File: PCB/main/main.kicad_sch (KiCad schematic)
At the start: 4 parts

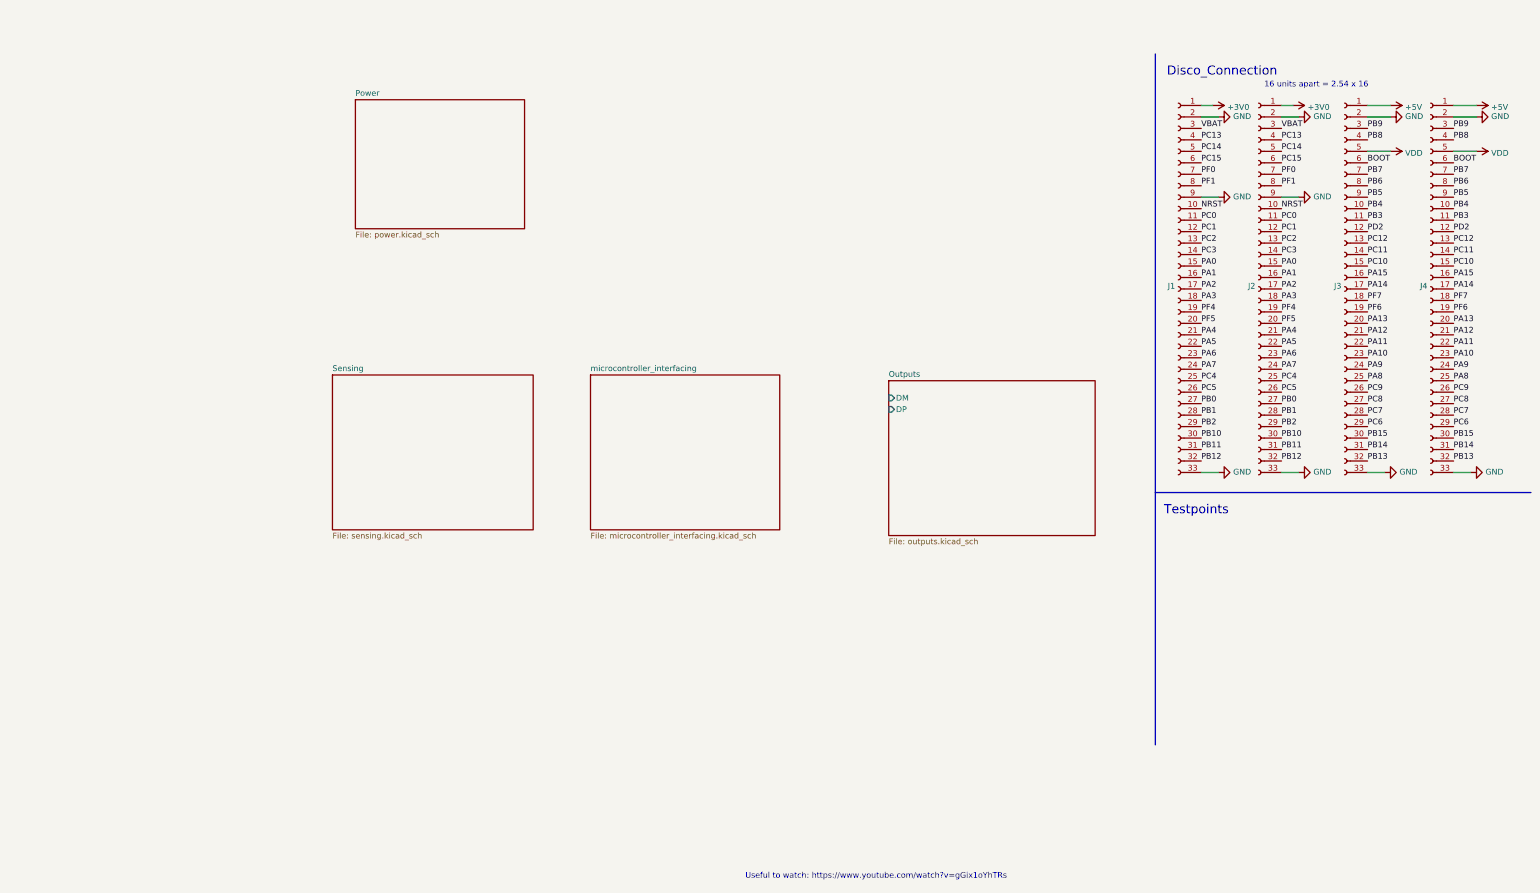
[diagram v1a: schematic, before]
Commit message: added digital sensors
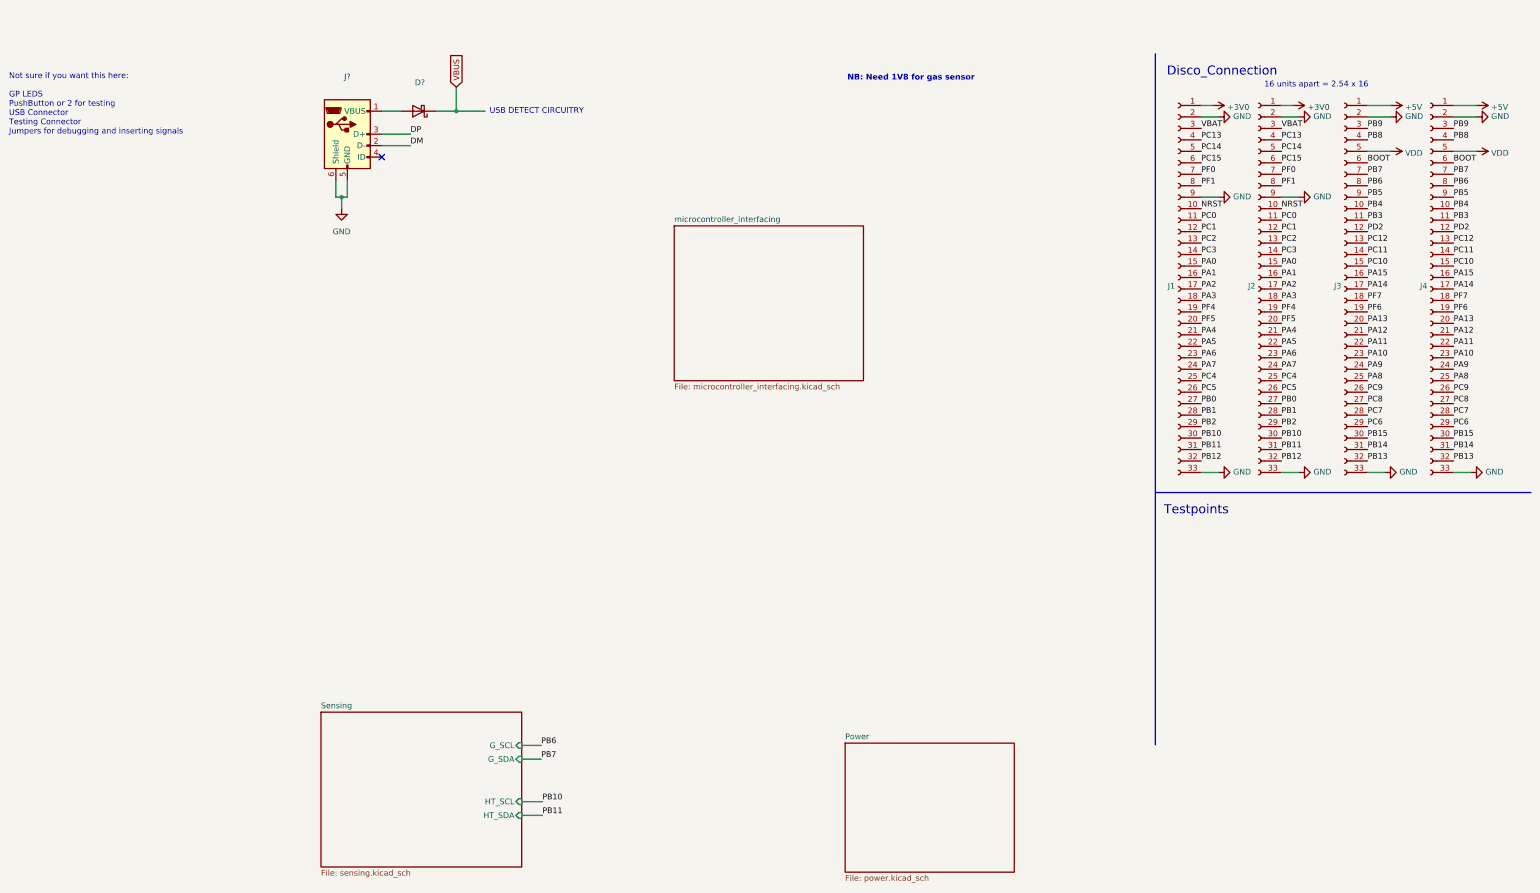
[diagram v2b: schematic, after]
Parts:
- added D?: (no value), symbol Device:D_Schottky
- added J?: (no value), symbol Connector:USB_B_Micro
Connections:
- net GND: now also J?.5 (GND), J?.6 (Shield)
- new net: D?.2 (A), J?.1 (VBUS)
- new net DM: J?.2 (D-)
- new net DP: J?.3 (D+)
- new net VBUS: D?.1 (K)
- no-connect marks 0 -> 1
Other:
- removed sheet Outputs
- sheet Sensing ports: added G_SCL, G_SDA, HT_SCL, HT_SDA; removed none
- note added: "NB: Need 1V8 for gas sensor"
- note added: "Not sure if you want this here: GP LEDS PushButton or 2 for testing USB Connector Testing Connector Jumpers for debugging and inserting signals"
- note added: "USB DETECT CIRCUITRY"
- note removed: "Useful to watch: https://www.youtube.com/watch?v=gGix1oYhTRs"
- title: EEE3088F Template -> DiscoverAir HAT

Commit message: added eeprom and some usb-uart connections
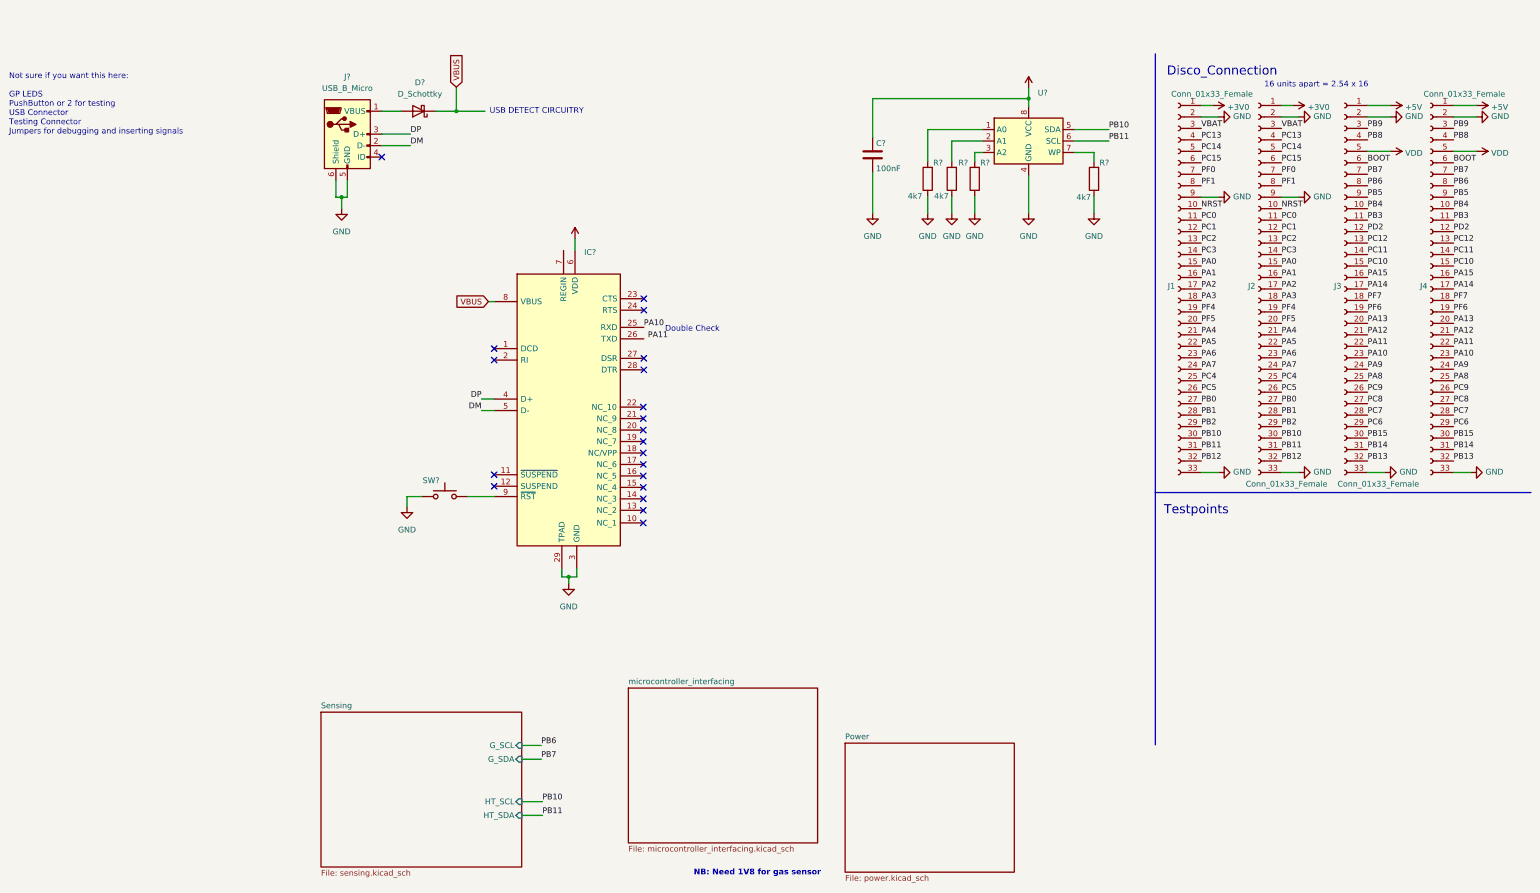
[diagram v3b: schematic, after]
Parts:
- added C?: 100nF, Capacitor_SMD:C_0603_1608Metric_Pad1.08x0.95mm_HandSolder, symbol Device:C
- added IC?: (no value), symbol CP2102-GMR:CP2102-GMR
- added R?: (no value), symbol Device:R
- added R? (x3): 4k7, Resistor_SMD:R_0603_1608Metric_Pad0.98x0.95mm_HandSolder, symbol Device:R
- added SW?: (no value), symbol Switch:SW_Push
- added U?: (no value), symbol Memory_EEPROM:CAT24C256
- D?: value (none) -> D_Schottky
- J1, J4: value (none) -> Conn_01x33_Female; footprint (none) -> Connector_PinHeader_2.54mm:PinHeader_1x33_P2.54mm_Vertical
- J2, J3: value (none) -> Conn_01x33_Female; footprint (none) -> Connector_PinSocket_2.54mm:PinSocket_1x33_P2.54mm_Vertical
- J?: value (none) -> USB_B_Micro
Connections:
- net DM: now also IC?.5 (D-)
- net DP: now also IC?.4 (D+)
- net GND: now also C?.2, IC?.29 (TPAD), IC?.3 (GND), R?.1, R?.1, R?.1, R?.1, SW?.1, U?.4 (GND)
- net PA10: now also IC?.25 (RXD)
- net PB10: now also U?.5 (SDA)
- net PB11: now also U?.6 (SCL)
- net VBUS: now also IC?.8 (VBUS)
- new net: IC?.9 (~{RST}), SW?.2
- new net: R?.2, U?.3 (A2)
- new net: R?.2, U?.2 (A1)
- new net: R?.2, U?.1 (A0)
- new net: R?.2, U?.7 (WP)
- new net +3V3: C?.1, IC?.6 (VDD), U?.8 (VCC)
- no-connect marks 1 -> 20
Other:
- note added: "Double Check"

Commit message: added ESD protection and updated USB IC
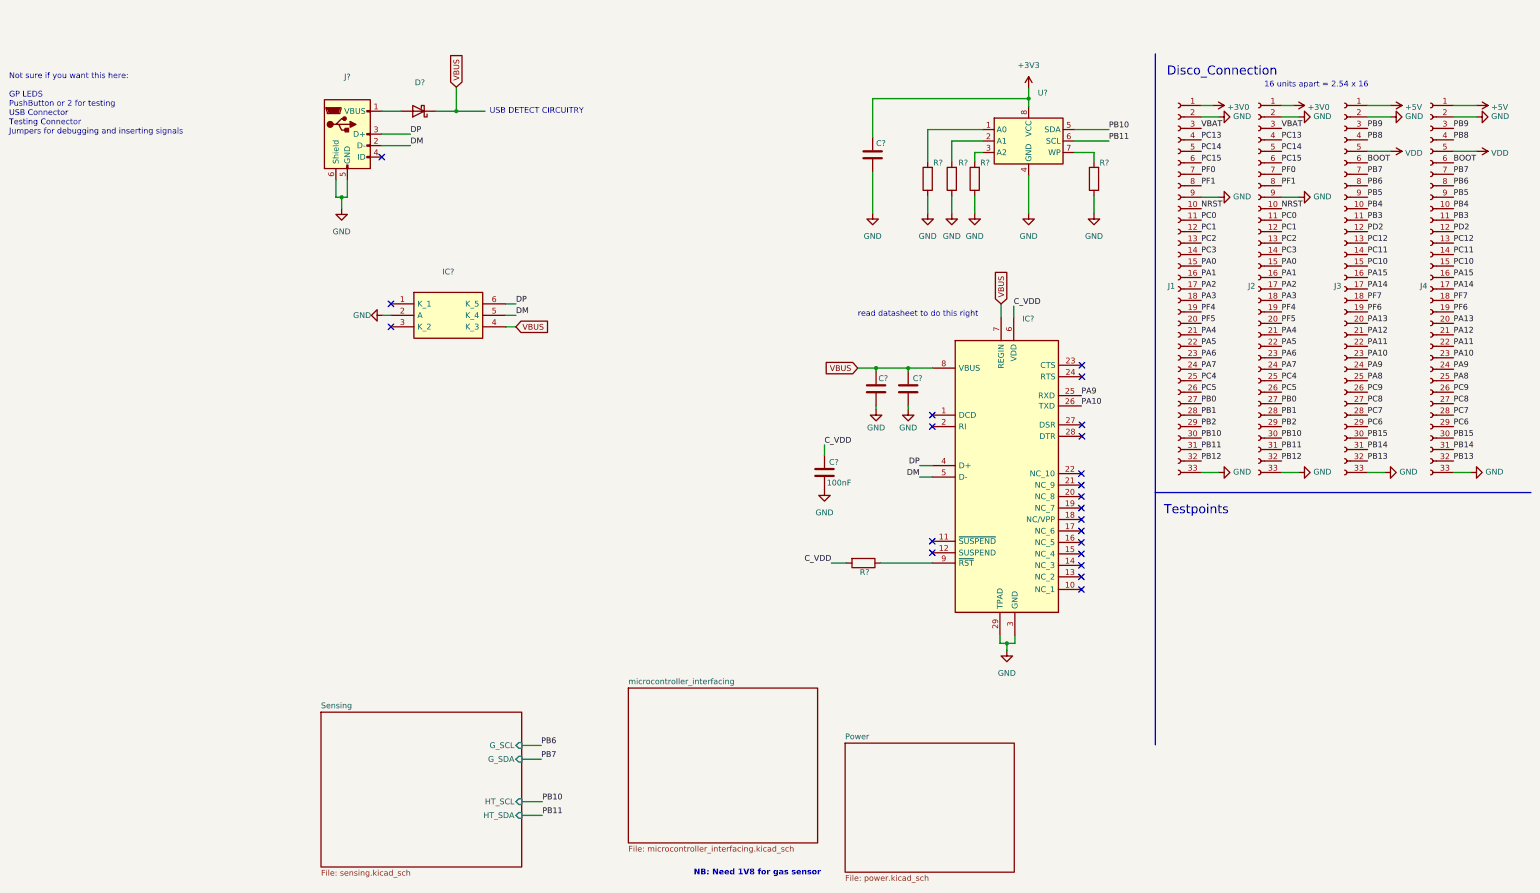
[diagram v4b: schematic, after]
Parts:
- removed SW?: (no value), symbol Switch:SW_Push
- added C? (x2): (no value), symbol Device:C
- added C?: 100nF, Capacitor_SMD:C_0603_1608Metric_Pad1.08x0.95mm_HandSolder, symbol Device:C
- added IC?: (no value), SOT65P210X110-6N, symbol SMF05CT1G:SMF05CT1G
- added R?: (no value), symbol Device:R
- C?: value 100nF -> (none); footprint Capacitor_SMD:C_0603_1608Metric_Pad1.08x0.95mm_HandSolder -> (none); Price (none) -> $0.0026
- D?: value D_Schottky -> (none)
- J1, J4: value Conn_01x33_Female -> (none); footprint Connector_PinHeader_2.54mm:PinHeader_1x33_P2.54mm_Vertical -> (none)
- J2, J3: value Conn_01x33_Female -> (none); footprint Connector_PinSocket_2.54mm:PinSocket_1x33_P2.54mm_Vertical -> (none)
- J?: value USB_B_Micro -> (none)
- R? (x3): value 4k7 -> (none); footprint Resistor_SMD:R_0603_1608Metric_Pad0.98x0.95mm_HandSolder -> (none)
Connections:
- net +3V3: no longer IC?.6 (VDD)
- net DM: now also IC?.5 (K_4)
- net DP: now also IC?.6 (K_5)
- net GND: now also C?.2, C?.2, C?.2, IC?.2 (A)
- net PA10: now also IC?.26 (TXD); no longer IC?.25 (RXD)
- net PA9: now also IC?.25 (RXD)
- net VBUS: now also IC?.7 (REGIN), C?.1, C?.1, IC?.4 (K_3)
- net at IC?.9 (~{RST}): now also R?.1
- new net C_VDD: C?.1, IC?.6 (VDD), R?.2
- no-connect marks 20 -> 22
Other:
- note added: "read datasheet to do this right"
- note removed: "Double Check"
- moved on the sheet: IC?

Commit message: layout started
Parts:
- added D2: D_Schottky, Diode_SMD:D_SMA, symbol Device:D_Schottky
- added J6: Conn_01x10_Male, Connector_PinHeader_2.54mm:PinHeader_1x10_P2.54mm_Vertical, symbol Connector:Conn_01x10_Male
- added Q1: Q_NMOS_GSD, Package_TO_SOT_SMD:SOT-23, symbol Device:Q_NMOS_GSD
- added R1, R2, R3: 4k7, Resistor_SMD:R_0603_1608Metric_Pad0.98x0.95mm_HandSolder, symbol Device:R
- C1: renamed from C?; value (none) -> 1uF; footprint (none) -> Capacitor_SMD:C_0603_1608Metric_Pad1.08x0.95mm_HandSolder
- C2, C4: renamed from C?; value (none) -> 100nF; footprint (none) -> Capacitor_SMD:C_0603_1608Metric_Pad1.08x0.95mm_HandSolder
- D1: renamed from D?; value (none) -> D_Schottky; footprint (none) -> Diode_SMD:D_SMA; LCSC (none) -> C2480
- IC1: renamed from IC?; value (none) -> SMF05CT1G; footprint SOT65P210X110-6N -> SMF05CT1G:SOT65P210X110-6N; LCSC (none) -> C15879; Price (none) -> $0.4054
- IC2: renamed from IC?; value (none) -> CP2102-GMR; footprint (none) -> CP2102-GMR:QFN50P500X500X100-29N-D; Arrow Part Number CP2102-GMR -> (none); Arrow Price/Stock https://www.arrow.com/en/products/cp2102-gmr/silicon-labs?r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 -> (none); LCSC (none) -> C6568; Manufacturer_Name Silicon Labs -> (none); Mouser Part Number 634-CP2102-GMR -> (none); Mouser Price/Stock https://www.mouser.co.uk/ProductDetail/Silicon-Labs/CP2102-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 -> (none); Price (none) -> $3.7227
- J1, J4: value (none) -> Conn_01x33_Female; footprint (none) -> Connector_PinHeader_2.54mm:PinHeader_1x33_P2.54mm_Vertical
- J2, J3: value (none) -> Conn_01x33_Female; footprint (none) -> Connector_PinSocket_2.54mm:PinSocket_1x33_P2.54mm_Vertical
- J5: renamed from J?; value (none) -> USB_B_Micro; footprint (none) -> MICROXNJ:SHOUHAN_MICROXNJ
- R4, R5, R6, R7, R8: renamed from R?; value (none) -> 4k7; footprint (none) -> Resistor_SMD:R_0603_1608Metric_Pad0.98x0.95mm_HandSolder
- U1: renamed from U?; value (none) -> CAT24C256; footprint (none) -> Package_SO:SOIC-8_3.9x4.9mm_P1.27mm
- gave numbers to parts that had none: 1
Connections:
- net +3V3 is gone; now on net +3V0: C4.1, U1.8 (VCC)
- net C_VDD is gone; now on net +3V0: C3.1, IC2.6 (VDD), R4.2
- net +3V0: now also C1.1, C2.1, IC2.7 (REGIN), R3.1
- net +5V: now also J6.1 (Pin_1)
- net GND: now also J6.10 (Pin_10), Q1.2 (S), R1.1
- net PA10: now also J6.9 (Pin_9)
- net PA9: now also J6.8 (Pin_8)
- net PB10: now also J6.6 (Pin_6)
- net PB11: now also J6.5 (Pin_5)
- net PB6: now also J6.4 (Pin_4)
- net PB7: now also J6.3 (Pin_3)
- net PC0: now also J6.7 (Pin_7), Q1.3 (D), R3.2
- net PC3: now also J6.2 (Pin_2)
- net VBUS: no longer C1.1, C2.1, IC2.7 (REGIN)
- net at D1.2 (A), J5.1 (VBUS): now also D2.2 (A)
- new net: Q1.1 (G), R2.1
- new net: D2.1 (K), R1.2, R2.2
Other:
- removed sheet microcontroller_interfacing
- sheet Power ports: added BATTERY_VOLTAGE; removed none
- note added: "ESD Protection"
- note added: "Memory Element and which pins you wish to use. debugging capabilities to test it"
- note added: "VBUS-VBAT-5V Connector"
- note removed: "NB: Need 1V8 for gas sensor"
- note removed: "USB DETECT CIRCUITRY"
- note removed: "read datasheet to do this right"
- moved on the sheet: C1, C2, C3, D1, IC1, IC2, J5, R4

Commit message: ver 1 complete
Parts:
- added D7, D8: (no value), symbol Device:LED
- added R24, R25, R26, R27: (no value), symbol Device:R
- added S1: (no value), symbol TS-1187A-B-A-B:TS-1187A-B-A-B
- C1: value 1uF -> (none); footprint Capacitor_SMD:C_0603_1608Metric_Pad1.08x0.95mm_HandSolder -> (none)
- C2, C3, C4: value 100nF -> (none); footprint Capacitor_SMD:C_0603_1608Metric_Pad1.08x0.95mm_HandSolder -> (none)
- D1, D2: value D_Schottky -> (none); footprint Diode_SMD:D_SMA -> (none)
- IC1: value SMF05CT1G -> (none); footprint SMF05CT1G:SOT65P210X110-6N -> (none)
- IC2: value CP2102-GMR -> (none); footprint CP2102-GMR:QFN50P500X500X100-29N-D -> (none)
- J1, J4: value Conn_01x33_Female -> (none); footprint Connector_PinHeader_2.54mm:PinHeader_1x33_P2.54mm_Vertical -> (none)
- J2, J3: value Conn_01x33_Female -> (none); footprint Connector_PinSocket_2.54mm:PinSocket_1x33_P2.54mm_Vertical -> (none); Alt_LCSC C12345 (example) -> (none); LCSC C1234 (example) -> (none)
- J5: value USB_B_Micro -> (none); footprint MICROXNJ:SHOUHAN_MICROXNJ -> (none)
- J6: value Conn_01x10_Male -> (none); footprint Connector_PinHeader_2.54mm:PinHeader_1x10_P2.54mm_Vertical -> (none)
- Q1: value Q_NMOS_GSD -> (none); footprint Package_TO_SOT_SMD:SOT-23 -> (none)
- R1, R2, R3, R4, R5, R6, R7, R8: value 4k7 -> (none); footprint Resistor_SMD:R_0603_1608Metric_Pad0.98x0.95mm_HandSolder -> (none)
- U1: value CAT24C256 -> (none); footprint Package_SO:SOIC-8_3.9x4.9mm_P1.27mm -> (none)
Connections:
- net +3V0: now also S1.A1 (COM_1)
- net GND: now also R24.2, R25.2, R26.2
- net PA2: now also D7.2 (A)
- net PA8: now also R27.2
- net PC13: now also D8.2 (A)
- net DM renamed DN
- new net: R26.1, R27.1, S1.B1 (COM_2)
- new net: D8.1 (K), R25.1
- new net: D7.1 (K), R24.1
- no-connect marks 22 -> 24
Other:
- note added: "ANALOG DATA READ"
- note added: "G_SCL"
- note added: "G_SDA"
- note added: "HT_SCL"
- note added: "HT_SDA"
- note added: "UART RX"
- note added: "UART TX"
- note added: "USB DETECT"
- moved on the sheet: C1, C2, C3, IC1, IC2, R4
